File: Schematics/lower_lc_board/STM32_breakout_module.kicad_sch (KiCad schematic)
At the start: 55 parts, among them J2 SWD_CONN, J3 USB_C_CONN, Q4 2N7002, SW1 SW_STM_RESET, SW2 SW_STM_BOOT_MODE, U5 STM32F103CBT6, U6 W25Q128JVS, U7 ISO1044BDR, U8 CP2102N-Axx-xQFN20, Y1 X322516MMB4SI

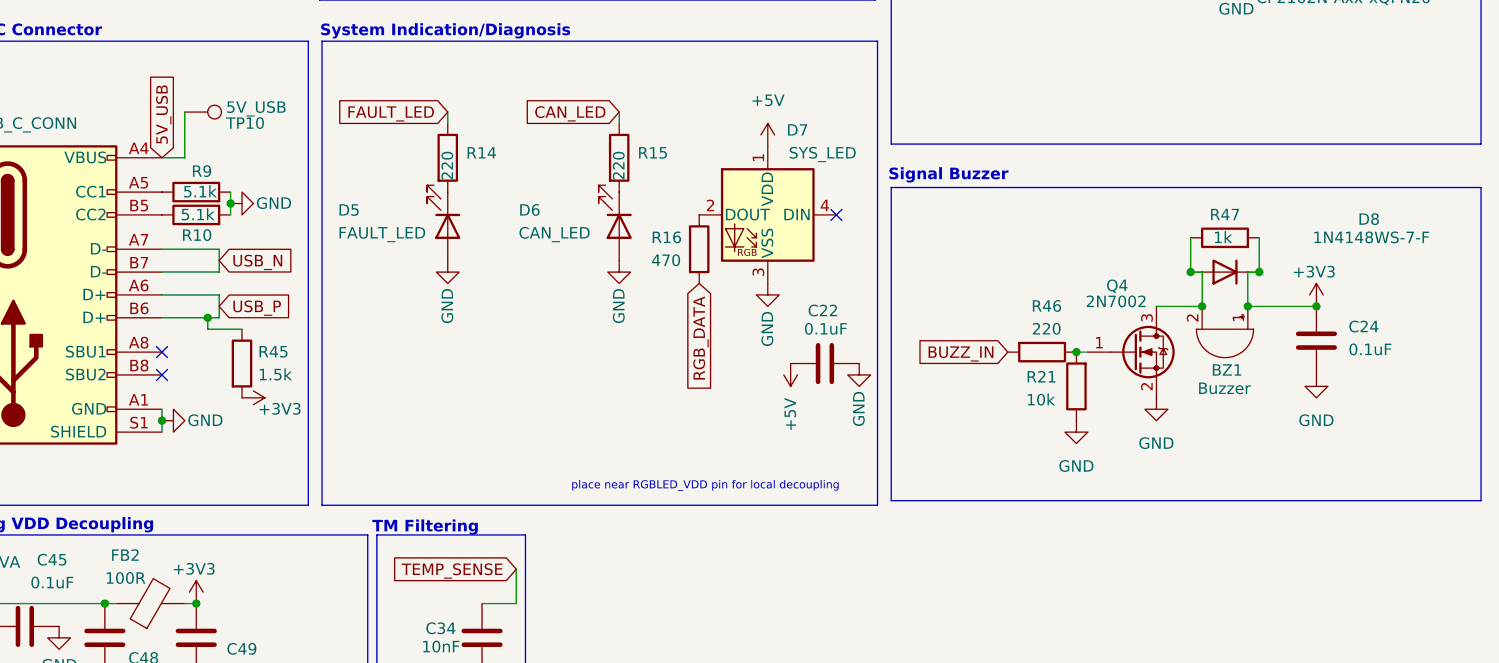
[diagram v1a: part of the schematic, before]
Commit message: lower refactor for review
 - curr using horziontal screw for TC
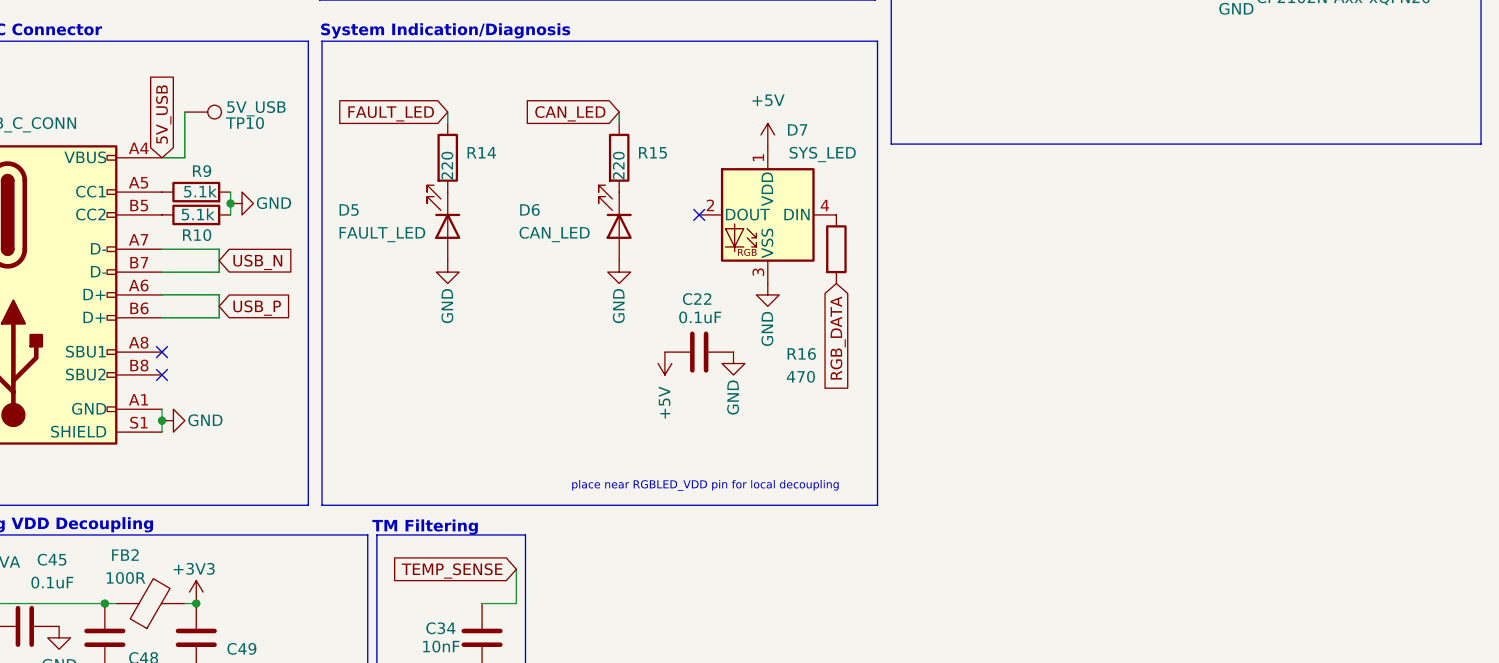
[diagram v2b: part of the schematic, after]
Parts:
- removed BZ1: Buzzer, Buzzer_Beeper:Buzzer_TDK_PS1240P02BT_D12.2mm_H6.5mm, symbol Device:Buzzer
- removed C24: 0.1uF, Capacitor_SMD:C_0603_1608Metric, symbol Device:C
- removed D8: 1N4148WS-7-F, Diode_SMD:D_SOD-323, symbol Diode:1N4148WS
- removed Q4: 2N7002, Package_TO_SOT_SMD:SOT-23, symbol Transistor_FET:2N7002
- removed R21: 10k, Resistor_SMD:R_0603_1608Metric, symbol Device:R
- removed R45: 1.5k, Capacitor_SMD:C_0402_1005Metric, symbol Device:R
- removed R46: 220, Resistor_SMD:R_0603_1608Metric, symbol Device:R
- removed R47: 1k, Resistor_SMD:R_0603_1608Metric, symbol Device:R
- R13: footprint Resistor_SMD:R_0603_1608Metric -> Resistor_SMD:R_0402_1005Metric; JLCPCB C4410 -> C11702
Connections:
- net at R16.1: now also D7.4 (DIN); no longer D7.2 (DOUT)
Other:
- note removed: "Signal Buzzer"
- moved on the sheet: C22, R16

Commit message: update backplane orientation
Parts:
- C21: LCSC (none) -> C96446
- U5: LCSC (none) -> C8304
- U6: LCSC (none) -> C97521
- U7: JLCPCB (none) -> C2878225
- U8: LCSC (none) -> C969913
- Y1: LCSC (none) -> C13738

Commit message: PCB for review
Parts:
- C10, C11: LCSC (none) -> C1634
- C13, C14: LCSC (none) -> C1525
- C15, C16, C17, C9: LCSC (none) -> C14663
- C20: LCSC (none) -> C52923
- C34: LCSC (none) -> C57112
- C48, C49: LCSC (none) -> C15849
- FB2: footprint Resistor_SMD:R_0805_2012Metric -> Resistor_SMD:R_0603_1608Metric; JLCPCB C1015 -> 1002; LCSC (none) -> 1002
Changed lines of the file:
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@@
 			)
 		)
+		(property "LCSC" "C14663"
+			(at 39.37 44.45 0)
+			(effects
+				(font
+					(size 1.27 1.27)
+				)
+				(hide yes)
+			)
+		)
 		(pin "1"
 		)
@@
 			)
 		)
+		(property "LCSC" "C14663"
+			(at 64.77 156.21 0)
+			(effects
+				(font
+					(size 1.27 1.27)
+				)
+				(hide yes)
+			)
+		)
 		(pin "1"
 		)
@@
 			)
 		)
+		(property "LCSC" "C15849"
+			(at 121.92 171.45 0)
+			(effects
+				(font
+					(size 1.27 1.27)
+				)
+				(hide yes)
+			)
+		)
 		(pin "2"
 		)
@@
 			)
 		)
+		(property "LCSC" "C1525"
+			(at 44.45 154.94 0)
+			(effects
+				(font
+					(size 1.27 1.27)
+				)
+				(hide yes)
+			)
+		)
 		(pin "1"
 		)
@@
 			)
 		)
+		(property "LCSC" "C14663"
+			(at 54.61 154.94 0)
+			(effects
+				(font
+					(size 1.27 1.27)
+				)
+				(hide yes)
+			)
+		)
 		(pin "1"
 		)
@@
 			)
 		)
-		(property "Footprint" "Resistor_SMD:R_0805_2012Metric"
+		(property "Footprint" "Resistor_SMD:R_0603_1608Metric"
 			(at 127 169.418 90)
 			(effects
@@
 			)
 		)
-		(property "JLCPCB" "C1015"
+		(property "JLCPCB" "1002"
 			(at 127 167.64 0)
 			(effects
@@
 			)
 		)
+		(property "LCSC" "1002"
+			(at 127 167.64 0)
+			(effects
+				(font
+					(size 1.27 1.27)
+				)
+				(hide yes)
+			)
+		)
 		(pin "2"
 		)
@@
 			)
 		)
+		(property "LCSC" "C14663"
+			(at 187.96 34.29 0)
+			(effects
+				(font
+					(size 1.27 1.27)
+				)
+				(hide yes)
+			)
+		)
 		(pin "1"
 		)
@@
 			)
 		)
+		(property "LCSC" "C57112"
+			(at 163.83 171.45 0)
+			(effects
+				(font
+					(size 1.27 1.27)
+				)
+				(hide yes)
+			)
+		)
 		(pin "1"
 		)
@@
 			)
 		)
+		(property "LCSC" "C15849"
+			(at 132.08 171.45 0)
+			(effects
+				(font
+					(size 1.27 1.27)
+				)
+				(hide yes)
+			)
+		)
 		(pin "2"
 		)
@@
 			)
 		)
+		(property "LCSC" "C1525"
+			(at 34.29 154.94 0)
+			(effects
+				(font
+					(size 1.27 1.27)
+				)
+				(hide yes)
+			)
+		)
 		(pin "1"
 		)
@@
 			)
 		)
+		(property "LCSC" "C52923"
+			(at 226.06 63.5 0)
+			(effects
+				(font
+					(size 1.27 1.27)
+				)
+				(hide yes)
+			)
+		)
 		(pin "1"
 		)
@@
 			)
 		)
+		(property "LCSC" "C1634"
+			(at 119.38 78.74 0)
+			(effects
+				(font
+					(size 1.27 1.27)
+				)
+				(hide yes)
+			)
+		)
 		(pin "1"
 		)
@@
 			(at 134.62 78.74 0)
 			(effects
+				(font
+					(size 1.27 1.27)
+				)
+				(hide yes)
+			)
+		)
+		(property "LCSC" "C1634"
+			(at 134.62 78.74 0)
+			(effects

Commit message: WIP - i2c-2 refactor
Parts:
- removed TP7: USB-DM, TestPoint:TestPoint_Pad_D1.0mm, symbol Connector:TestPoint
- removed TP8: USB-DP, TestPoint:TestPoint_Pad_D1.0mm, symbol Connector:TestPoint
- C10, C11: JLCPCB C1634 -> (none)
- C13, C14: JLCPCB C1525 -> (none)
- C15, C16, C17, C18, C19, C9: JLCPCB C14663 -> (none)
- C20: JLCPCB C52923 -> (none)
- C21: JLCPCB C96446 -> (none)
- C22, C45: JLCPCB C14663 -> (none); LCSC (none) -> C14663
- C34: JLCPCB C57112 -> (none)
- C48, C49: JLCPCB C15849 -> (none)
- D5: value FAULT_LED -> DB_LED (YLW); JLCPCB C2290 -> (none); LCSC C2286 -> C72038
- D6: value CAN_LED -> CAN_LED (WHT); JLCPCB C2290 -> (none)
- FB2: JLCPCB 1002 -> (none)
- J3: JLCPCB C5178541 -> (none); LCSC (none) -> C5178541
- R10, R9: JLCPCB C23186 -> (none)
- R11: JLCPCB C25768 -> (none); LCSC (none) -> C25768
- R12: JLCPCB C25792 -> (none); LCSC (none) -> C25792
- R13: JLCPCB C11702 -> (none); LCSC (none) -> C11702
- R14: value 220 -> 680; JLCPCB C22962 -> (none); LCSC C22962 -> C23228
- R15: value 220 -> 270; JLCPCB C22962 -> (none); LCSC C22808 -> C22966
- R16: JLCPCB C23179 -> (none); LCSC (none) -> C23179
- R48, R5, R6, R60, R7, R8: JLCPCB C25804 -> (none); LCSC (none) -> C25804
- SW1, SW2: JLCPCB C318884 -> (none); LCSC (none) -> C318884
- U5: JLCPCB C8304 -> (none)
- U6: JLCPCB C97521 -> (none)
- U7: JLCPCB C2878225 -> (none)
- U8: JLCPCB C969913 -> (none)
- Y1: JLCPCB C13738 -> (none)
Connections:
- net FAULT_LED is gone; now on net DB_LED: R14.1, U5.29 (PA8)
- net USART_RX: now also U5.31 (PA10); no longer U5.22 (PB11)
- net USART_TX: now also U5.30 (PA9); no longer U5.21 (PB10)
- net VSOL-SW: now also U5.33 (PA12); no longer U5.31 (PA10)
- net DB_LED: now reaches U5.32 (PA11)
- net HALL_SCL renamed HALL_SCL1
- net HALL_SDA renamed HALL_SDA1
- new net HALL_SCL2: U5.21 (PB10)
- new net HALL_SDA2: U5.22 (PB11)
- no-connect marks 19 -> 18
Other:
- note removed: "usart3"
- note removed: "usb DM/DP"

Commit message: start routing for new bus
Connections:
- net DB_LED: no longer U5.32 (PA11)
- no-connect marks 18 -> 19
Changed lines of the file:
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@@
+	)
+	(no_connect
+		(at 74.93 76.2)
 	)
 	(no_connect
@@
 			(effects
 				(font
-					(size 1.27 1.27)
-				)
-				(justify left)
-				(hide yes)
-			)
-		)
-	)
-	(global_label "DB_LED"
-		(shape input)
-		(at 74.93 76.2 0)
-		(fields_autoplaced yes)
-		(effects
-			(font
-				(size 1.27 1.27)
-			)
-			(justify left)
-		)
-		(property "Intersheetrefs" "${INTERSHEET_REFS}"
-			(at 84.8699 76.2 0)
-			(effects
-				(font

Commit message: start 2nd refactor
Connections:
- net VSOL-SW: now also U5.32 (PA11); no longer U5.33 (PA12)
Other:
- note added: "I2C-2"
- note added: "usart-1"
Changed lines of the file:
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@@
-	)
-	(no_connect
-		(at 74.93 76.2)
 	)
 	(no_connect
@@
 	(no_connect
 		(at 41.91 71.12)
+	)
+	(no_connect
+		(at 74.93 78.74)
 	)
 	(no_connect
@@
 	(text "* needs software remap"
 		(exclude_from_sim no)
-		(at 25.654 101.6 90)
+		(at 25.146 92.964 90)
 		(effects
 			(font
@@
 		)
 	)
+	(text "usart-1"
+		(exclude_from_sim no)
+		(at 92.202 72.136 0)
+		(effects
+			(font
+				(size 1.27 1.27)
+				(color 0 0 0 1)
+			)
+		)
+	)
 	(text "VBAT & VDD Decoupling"
 		(exclude_from_sim no)
@@
 		(exclude_from_sim no)
 		(at 23.876 84.074 0)
+		(effects
+			(font
+				(size 0.762 0.762)
+				(color 0 0 0 1)
+			)
+		)
+	)
+	(text "I2C-2"
+		(exclude_from_sim no)
+		(at 26.162 103.378 0)
 		(effects
 			(font
@@
 		)
 	)
-	(global_label "VSOL-SW"
-		(shape input)
-		(at 74.93 78.74 0)
-		(fields_autoplaced yes)
-		(effects
-			(font
-				(size 1.27 1.27)
-			)
-			(justify left)
-		)
-		(property "Intersheetrefs" "${INTERSHEET_REFS}"
-			(at 86.8052 78.74 0)
-			(effects
-				(font
-					(size 1.27 1.27)
-				)
-				(justify left)
-				(hide yes)
-			)
-		)
-	)
 	(global_label "SPI_MISO"
 		(shape input)
@@
 			(effects
 				(font
+					(size 1.27 1.27)
+				)
+				(justify left)
+				(hide yes)
+			)
+		)
+	)
+	(global_label "VSOL-SW"
+		(shape input)
+		(at 74.93 76.2 0)
+		(fields_autoplaced yes)
+		(effects
+			(font
+				(size 1.27 1.27)
+			)
+			(justify left)
+		)
+		(property "Intersheetrefs" "${INTERSHEET_REFS}"
+			(at 86.8052 76.2 0)
+			(effects
+				(font

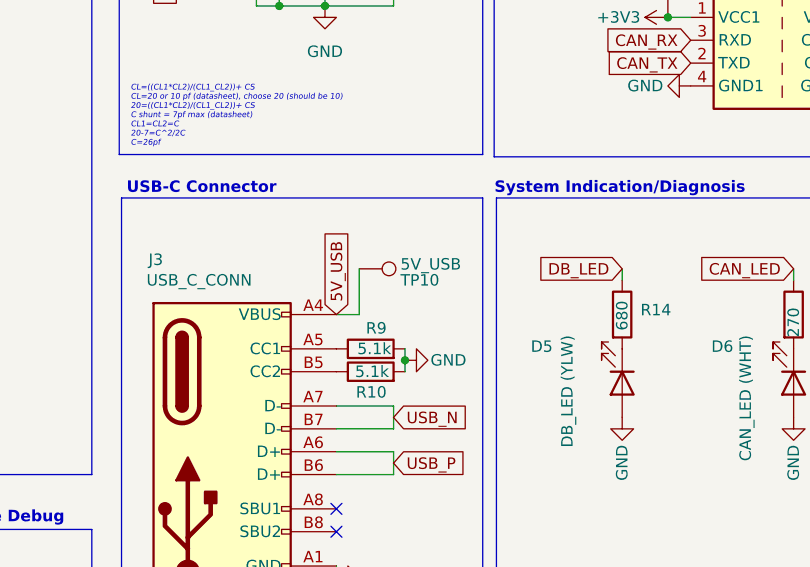
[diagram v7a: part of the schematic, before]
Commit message: silkscreen and new i2c bus
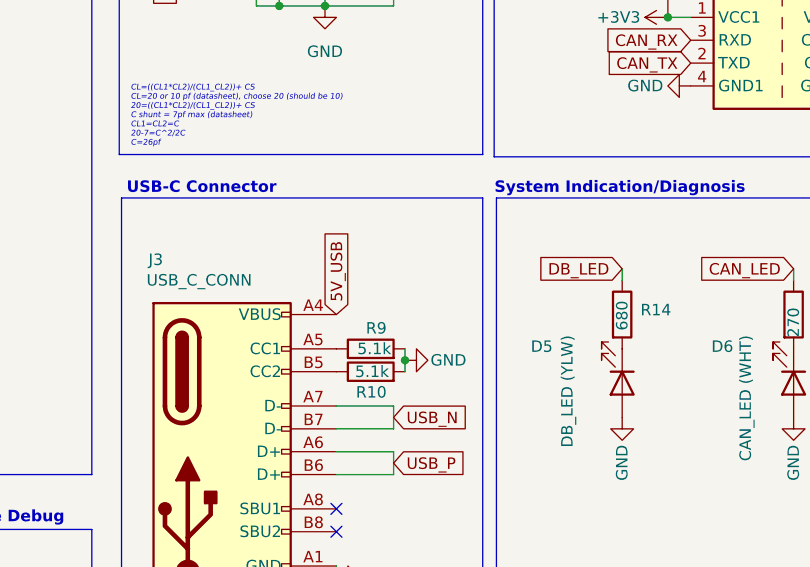
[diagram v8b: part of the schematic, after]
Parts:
- removed TP10: 5V_USB, TestPoint:TestPoint_Pad_D1.0mm, symbol Connector:TestPoint
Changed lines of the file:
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@@
 	(wire
 		(pts
-			(xy 128.27 118.11) (xy 130.81 118.11)
-		)
-		(stroke
-			(width 0)
-			(type default)
-		)
-	)
-	(wire
-		(pts
 			(xy 165.1 85.09) (xy 167.64 85.09)
 		)
@@
 		)
 	)
-	(wire
-		(pts
-			(xy 130.81 118.11) (xy 130.81 113.03)
-		)
-		(stroke
-			(width 0)
-			(type default)
-		)
-	)
 	(rectangle
 		(start 104.14 61.595)
@@
 					(unit 1)
 				)
-			)
-		)
-	)
-	(symbol
-		(lib_id "Connector:TestPoint")
-		(at 130.81 113.03 270)
-		(unit 1)
-		(exclude_from_sim no)
-		(in_bom yes)
-		(on_board yes)
-		(dnp no)
-		(property "Reference" "TP10"
-			(at 135.382 114.3 90)
-			(effects
-				(font
-					(size 1.27 1.27)
-				)
-				(justify left)
-			)
-		)
-		(property "Value" "5V_USB"
-			(at 135.382 112.522 90)
-			(effects
-				(font
-					(size 1.27 1.27)
-				)
-				(justify left)
-			)
-		)
-		(property "Footprint" "TestPoint:TestPoint_Pad_D1.0mm"
-			(at 130.81 118.11 0)
-			(effects
-				(font
-					(size 1.27 1.27)
-				)
-				(hide yes)
-			)
-		)
-		(property "Datasheet" "~"
-			(at 130.81 118.11 0)
-			(effects
-				(font
-					(size 1.27 1.27)
-				)
-				(hide yes)
-			)
-		)
-		(property "Description" "test point"
-			(at 130.81 113.03 0)
-			(effects
-				(font
-					(size 1.27 1.27)
-				)
-				(hide yes)
-			)
-		)
-		(property "Sim.Device" ""
-			(at 130.81 113.03 0)
-			(effects
-				(font
-					(size 1.27 1.27)
-				)
-				(hide yes)
-			)
-		)
-		(property "Sim.Pins" ""
-			(at 130.81 113.03 0)
-			(effects
-				(font
-					(size 1.27 1.27)
-				)
-				(hide yes)
-			)
-		)
-		(pin "1"
-		)
-		(instances
-			(project "lower_lc_board"
-				(path "/d63798c4-e363-437e-9012-e4aff32e6642/925ef91a-c900-4b94-a159-606c279d7192"
-					(reference "TP10")
-					(unit 1)
-				)
